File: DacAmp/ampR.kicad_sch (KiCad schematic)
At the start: 1 part, among them U2 NE5532

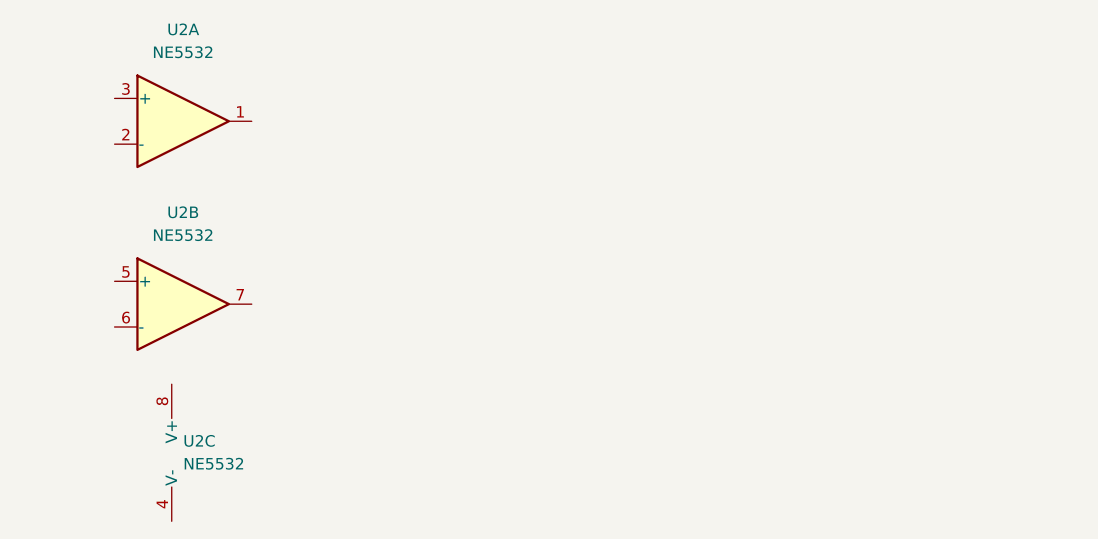
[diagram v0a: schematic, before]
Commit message: add op amps to ampR
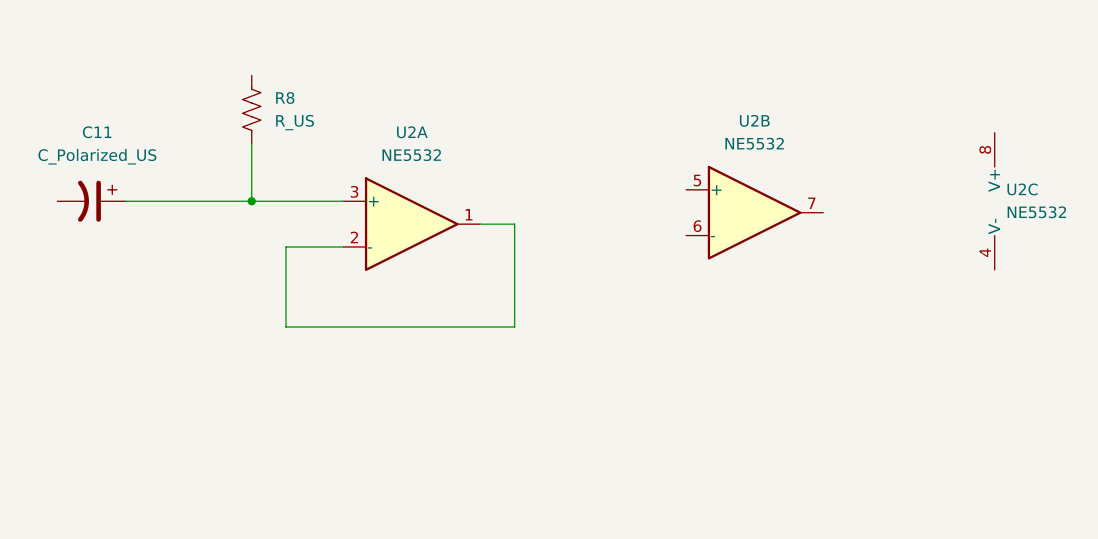
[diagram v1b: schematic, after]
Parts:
- added C11: C_Polarized_US, symbol Device:C_Polarized_US
- added R8: R_US, symbol Device:R_US
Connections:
- net at U2.1: now also U2.2 (-)
- net at U2.3 (+): now also C11.1, R8.2

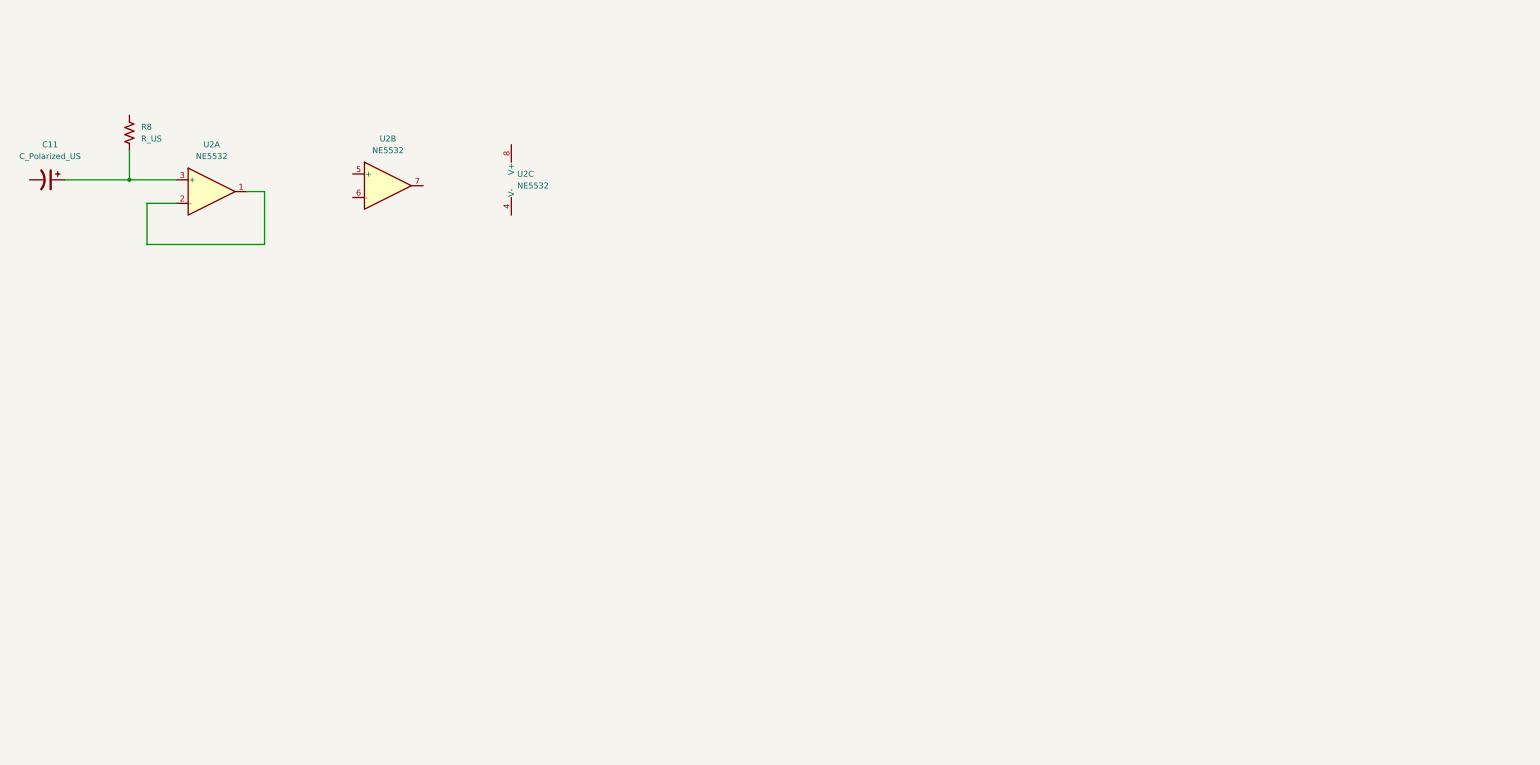
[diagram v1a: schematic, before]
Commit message: add basic amp architecture
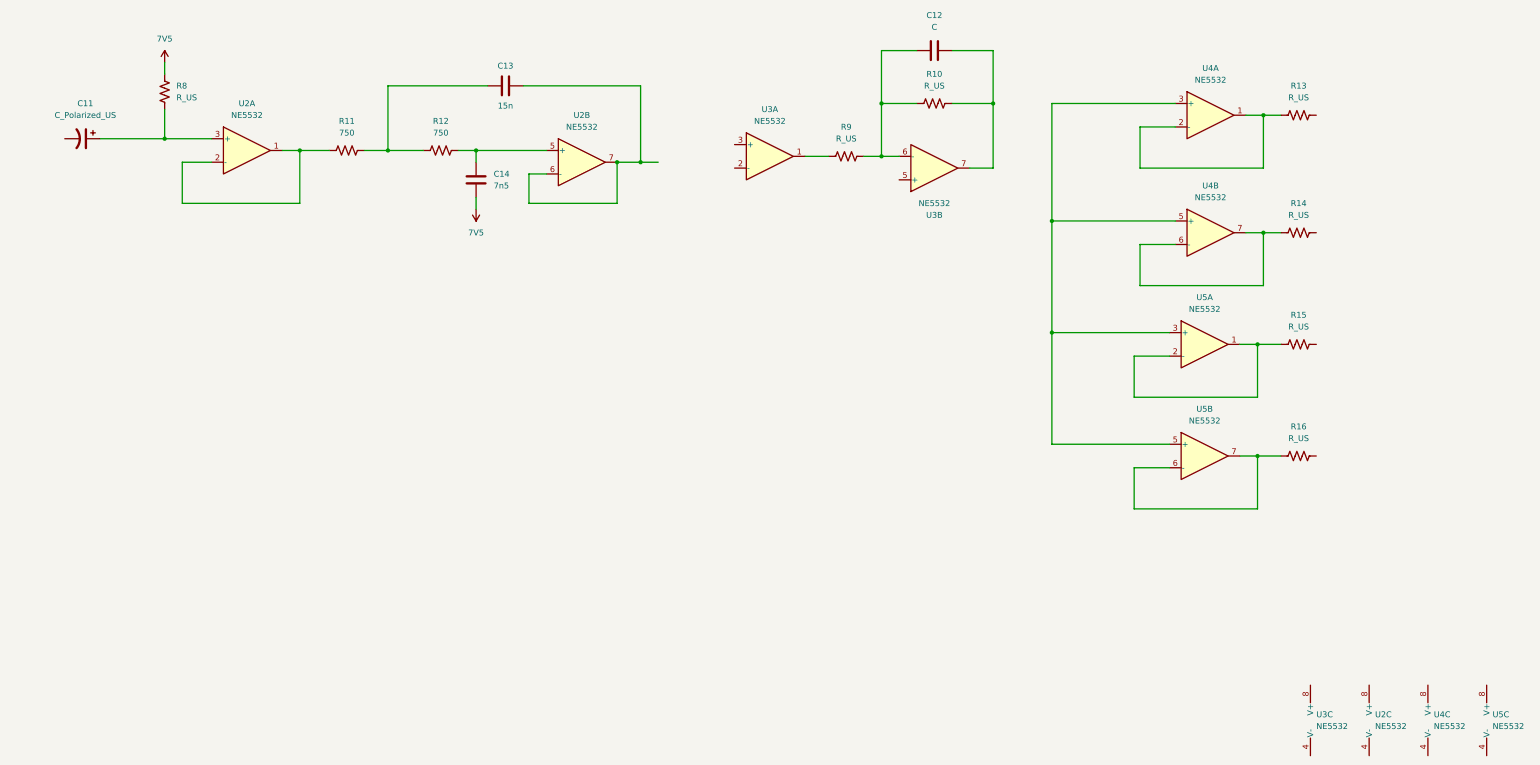
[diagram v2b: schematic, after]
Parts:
- added C12: C, symbol Device:C
- added C13: 15n, symbol Device:C
- added C14: 7n5, symbol Device:C
- added R10, R13, R14, R15, R16, R9: R_US, symbol Device:R_US
- added R11, R12: 750, symbol Device:R_US
- added U3, U4, U5: NE5532, symbol Amplifier_Operational:NE5532
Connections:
- net at U2.5 (+): now also C14.1, R12.2
- net at U2.6 (-): now also U2.7, C13.2
- net at U2.1, U2.2 (-): now also R11.1
- net 7V5: now reaches R8.1
- net 7V5: now also C14.2
- new net: R16.1, U5.6 (-), U5.7
- new net: R9.1, U3.1
- new net: R13.1, U4.1, U4.2 (-)
- new net: C12.1, R10.1, R9.2, U3.6 (-)
- new net: C12.2, R10.2, U3.7
- new net: R15.1, U5.1, U5.2 (-)
- new net: U4.3 (+), U4.5 (+), U5.3 (+), U5.5 (+)
- new net: C13.1, R11.2, R12.1
- new net: R14.1, U4.6 (-), U4.7
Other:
- moved on the sheet: C11, R8, U2A, U2B, U2C
